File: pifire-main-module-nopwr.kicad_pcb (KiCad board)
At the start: 2 copper layers, 65 x 56 mm, 40 parts, among them J1 GPIO, J10 Relay_Fan_JST, J11 AUX GPIO_PWR, J12 5V_ONOFF, J13 1WIRE_TEST, J14 PWR_SW, J15 BUTTONS_ENCODER, J2 SPI_DISPLAY, J4 12V_IN, J5 5V_IN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

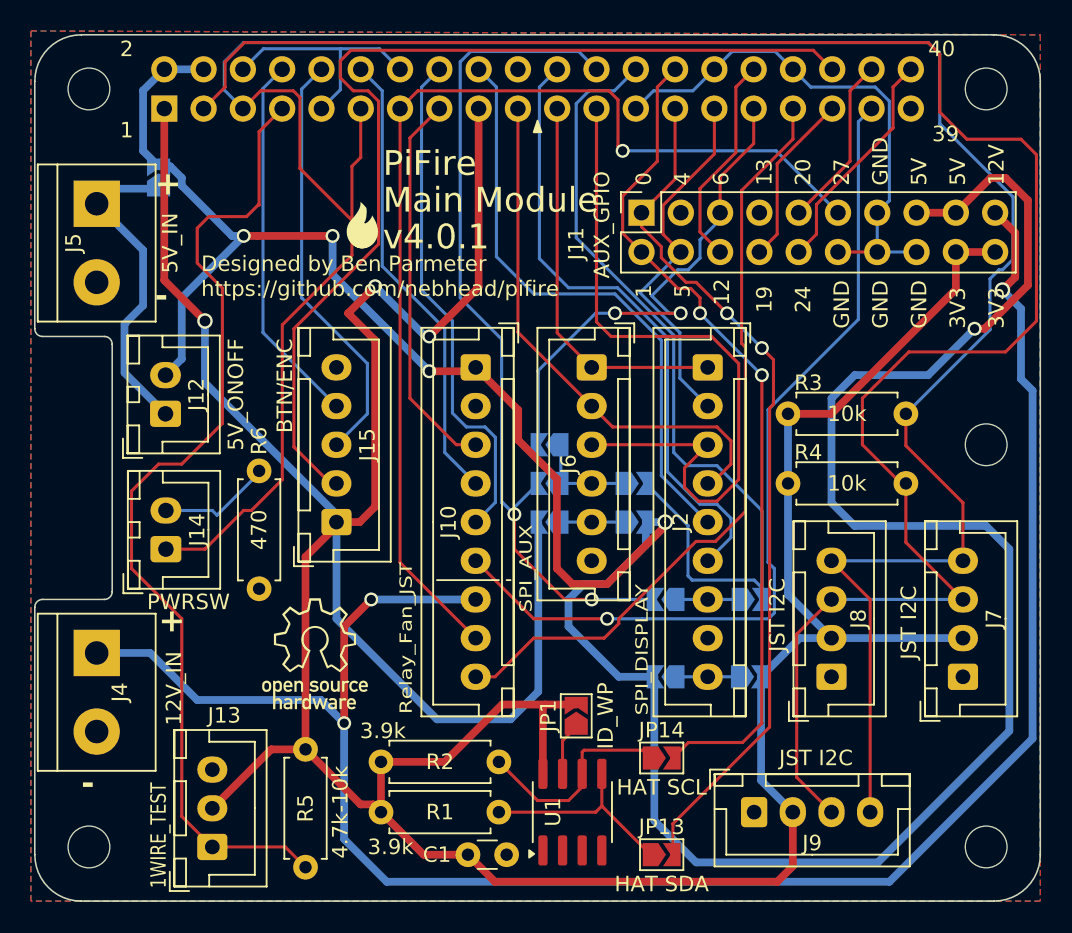
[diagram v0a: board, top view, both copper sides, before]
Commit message: Updated to v4.0.2
Split PWM pins out of the Relay/Fan header to create two headers.  This makes the board design more modular going forward and makes it easier to source the smaller 6 pin JST header.
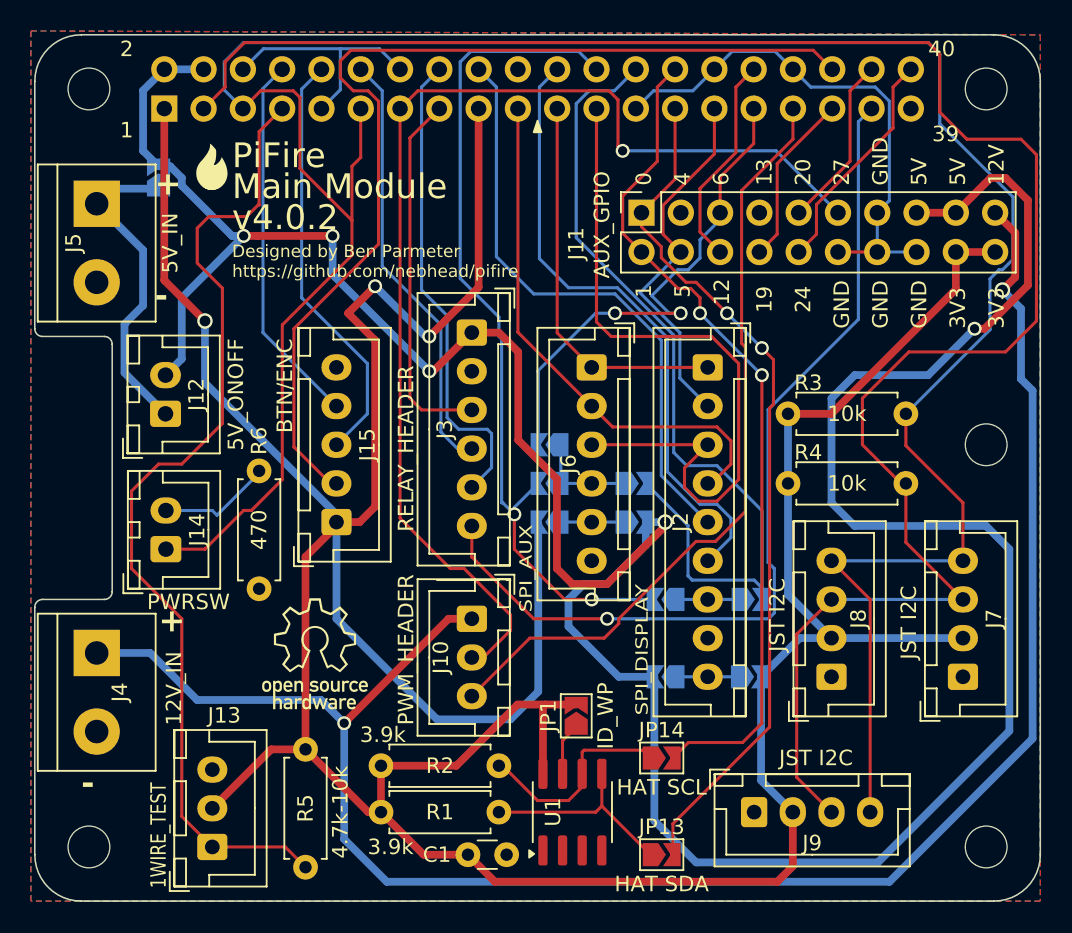
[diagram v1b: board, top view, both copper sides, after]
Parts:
- added J3: RELAY_HEADER, Connector_JST:JST_XH_B6B-XH-A_1x06_P2.50mm_Vertical, F.Cu at (128.2, 63.2)
- J10: value Relay_Fan_JST -> PWM_HEADER; footprint Connector_JST:JST_XH_B9B-XH-A_1x09_P2.50mm_Vertical -> Connector_JST:JST_XH_B3B-XH-A_1x03_P2.50mm_Vertical
- moved J10 16.3 mm to (128.2, 81.8)
- moved R2 0.25 mm to (122.4, 91.2)
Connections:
- J10 pad 1: 5V -> +12V
- J10 pad 2: GND -> GPIO27
- J10 pad 3: R_PWR -> PWM
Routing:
- net +12V: track 126.0 -> 121.6 mm, vias 3 -> 2
- net GPIO27: track 70.3 -> 74.5 mm
- net 5V: track 189.4 -> 193.5 mm
- net R_FAN: track 56.6 -> 58.9 mm
- net R_AUG: track 33.0 -> 31.0 mm
- net R_IGN: track 29.8 -> 28.0 mm
- net R_PWR: track 25.0 -> 23.8 mm
- net PWM: track 49.6 -> 50.3 mm
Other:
- board text added: "v4.0.2"
- board text removed: "v4.0.1"
